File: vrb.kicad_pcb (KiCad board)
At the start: 6 copper layers, 82 x 75 mm, 217 parts, among them J1 SM04B-GHS, J10 MiniFit, J11 XT30, J12 Mezzanine, J13 MiniFit, J14 Conn_01x02, J2 SM04B-GHS, J3 MiniFit, J4 MiniFit, J5 Pixhawk 1, J6 Pixhawk 2, J7 SM04B-GHS, J8 DEBUG, J9 SM04B-GHS, Q1 Q_NMOS_GSD, Q2 Q_NMOS_GSD, U1 STM32G0B1CBUx, U10 INA180A2, U11 TJA1051TK/3/1J, U12 I3A4W008A033V-001-R, U13 INA180A2, U14 TPS2121, U15 TPS2121, U16 TLV71333PDBVR, U17 TLA2528, U18 TPS2116DRL, U2 TJA1051TK/3/1J, U3 LMR51635, U4 INA180A2, U5 LMR51635, U6 INA180A2, U7 LMR51635, U8 INA180A2, U9 LMR51635, Y1 XRCGB16M000FXN20R0

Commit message: improvements with derick
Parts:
- added D22: 15V, Diode_SMD:D_SOD-523, F.Cu at (116.7, 126.5)
- added Q3: MMBT5551L, Package_TO_SOT_SMD:SOT-23, F.Cu at (120.2, 127.6)
- added Q4: FDC5614P, Package_TO_SOT_SMD:TSOT-23-6, F.Cu at (139.8, 122.9)
- added R84: 10K, Resistor_SMD:R_0402_1005Metric, F.Cu at (120.3, 130.7)
- added R85: 1K, Resistor_SMD:R_0402_1005Metric, F.Cu at (123.2, 128.8)
- added TP10: TestPoint, TestPoint:TestPoint_Pad_1.0x1.0mm, F.Cu at (99.9, 129.3)
- added TP12: GND, TestPoint:TestPoint_Loop_D2.50mm_Drill1.0mm, F.Cu at (85.0, 65.0)
- D11, D4, D5, D6, D7: value BLUE -> GREEN
- R43: value Rup -> 8K2
- R78: value 330 -> 24K
- moved R81 1.25 mm to (143.4, 119.3)
- moved R82 1.25 mm to (143.4, 120.9)
- moved R83 1.25 mm to (143.4, 122.5)
- moved TP11 1.25 mm to (146.4, 122.0)
- moved D20 0.30 mm to (118.2, 130.8)
- moved R78 0.30 mm to (117.7, 132.2)
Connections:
- D20 pad 2: /FAULT -> Net-(D20-A)
- U1 pad 29: /FAULT -> /nFAULT
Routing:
- net Net-(D22-K): track 0.00 -> 30.5 mm, vias 0 -> 2
- net Net-(D20-A): track 0.00 -> 25.8 mm, vias 0 -> 2
- net /FAULT: track 9.91 -> 0.00 mm
- net /nFAULT: track 0.00 -> 6.31 mm
- net +3V3: track 340.4 -> 343.2 mm
- net GND: track 111.9 -> 114.6 mm, vias 149 -> 151
- net /RESV2: track 58.4 -> 60.2 mm
- net Net-(Q3-B): track 0.00 -> 1.68 mm
- net +BATT: track 0.78 -> 1.47 mm, vias 22 -> 24
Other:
- board text added: "GND"

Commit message: final export of r1 after changes
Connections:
- net /IPAYLOAD renamed /IPAYLOAD1
- net /RESV0 renamed /IPAYLOAD2
- net /RESV1 renamed /IPAYLOAD3
- net /RESV2 renamed /VBAT_SCALED

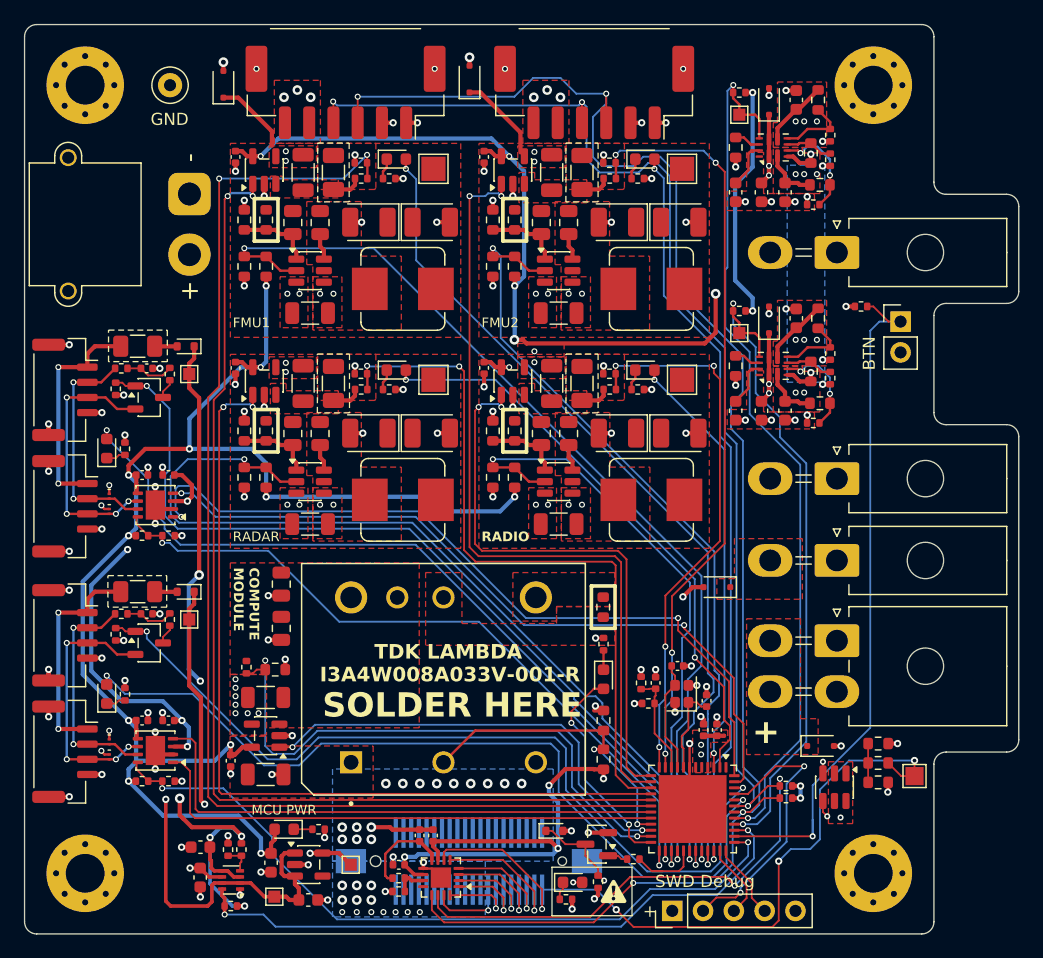
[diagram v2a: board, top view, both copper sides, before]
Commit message: updated layout for fault led with new circuit, rerouted
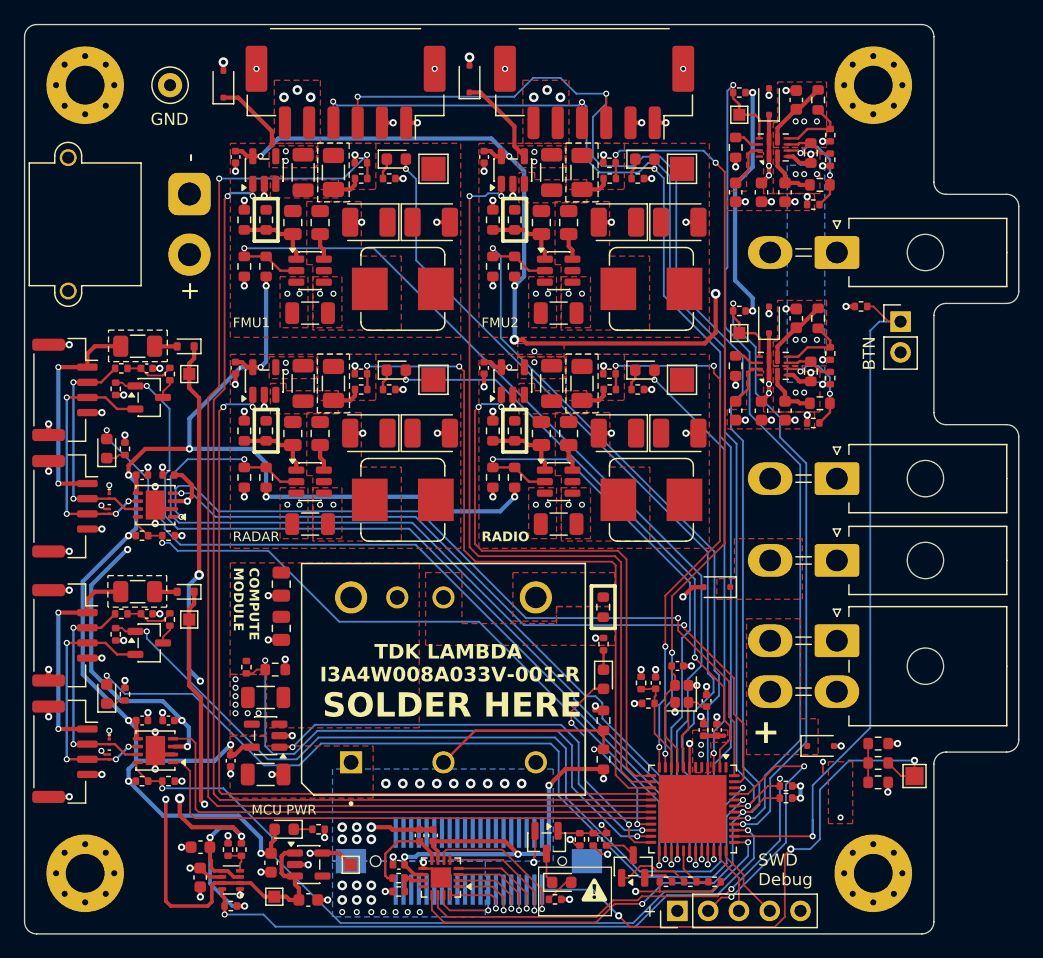
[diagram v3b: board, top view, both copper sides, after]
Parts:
- removed D22: 15V, Diode_SMD:D_SOD-523
- removed the Q4 at (139.8, 122.9)
- added Q3: BSS123, Package_TO_SOT_SMD:SOT-23, F.Cu at (116.0, 127.4)
- added R76: 200K, Resistor_SMD:R_0402_1005Metric, F.Cu at (119.9, 127.2)
- added R78: 1K, Resistor_SMD:R_0402_1005Metric, F.Cu at (121.0, 127.2)
- added R81: 20K, Resistor_SMD:R_0402_1005Metric, F.Cu at (129.9, 130.7)
- added R82: 180, Resistor_SMD:R_0402_1005Metric, F.Cu at (125.9, 130.7)
- R79: renamed from R84; value 10K -> 68K
- R80: renamed from R85; value 1K -> 5K
- moved R80 5.06 mm to (127.9, 130.7)
- moved R79 3.81 mm to (118.8, 127.2)
- moved Q4 3.52 mm to (123.2, 129.4), turned to 90 degrees
- moved D20 0.90 mm to (117.3, 130.8)
- moved R77 0.90 mm to (116.8, 132.2)
- moved J14 0.42 mm to (126.8, 133.1)
- renumbered C38 to C1, C7 to C10, C8 to C11, C48 to C12, C9 to C13, C10 to C14, C11 to C15, C12 to C16, C13 to C17, C49 to C18, C14 to C19, C39 to C2, C15 to C20, C16 to C21, C17 to C22, C18 to C23, C50 to C24, C19 to C25, C20 to C26, C21 to C27, C22 to C28, C23 to C29, C1 to C3, C51 to C30, C24 to C31, C25 to C32, C26 to C33, C27 to C34, C28 to C35, C29 to C36, C33 to C37, C34 to C38, C36 to C39, C2 to C4, C35 to C40, C30 to C41, C31 to C42, C37 to C43, C32 to C44, C44 to C45, C42 to C47, C54 to C48, C55 to C49, C3 to C5, C57 to C50, C43 to C51, C45 to C52, C40 to C53, C41 to C54, C47 to C6, C4 to C7, C5 to C8, C6 to C9, D9 to D10, D10 to D11, D19 to D12, D11 to D13, D13 to D14, D12 to D15, D15 to D16, D14 to D17, D16 to D18, D21 to D19, D18 to D21, D17 to D4, D4 to D5, D5 to D6, D6 to D7, D7 to D8, D8 to D9, J11 to J1, J5 to J10, J10 to J11, J6 to J12, J8 to J14, J12 to J2, J14 to J3, J1 to J4, J2 to J5, J7 to J6, J9 to J7, J4 to J8, J3 to J9, Q3 to Q4, R79 to R1, R9 to R10, R10 to R11, R11 to R12, R12 to R13, R13 to R14, R14 to R15, R15 to R16, R16 to R17, R17 to R18, R18 to R19, R1 to R2, R19 to R20, R20 to R21, R21 to R22, R22 to R23, R23 to R24, R24 to R25, R25 to R26, R26 to R27, R27 to R28, R28 to R29, R2 to R3, R29 to R30, R30 to R31, R31 to R32, R32 to R33, R33 to R34, R34 to R35, R35 to R36, R36 to R37, R37 to R38, R38 to R39, R3 to R4, R39 to R40, R40 to R41, R41 to R42, R42 to R43, R43 to R47, R4 to R5, R61 to R53, R62 to R54, R63 to R55, R64 to R56, R65 to R57, R66 to R58, R67 to R59, R5 to R6, R68 to R60, R56 to R61, R58 to R62, R59 to R63, R54 to R64, R57 to R65, R60 to R66, R53 to R67, R55 to R68, R73 to R69, R6 to R7, R75 to R70, R47 to R71, R69 to R72, R81 to R73, R82 to R74, R83 to R75, R78 to R77, R7 to R8, R71 to R83, R72 to R84, R74 to R85, R70 to R86, R77 to R87, R76 to R88, R8 to R9, TP12 to TP1, TP11 to TP10, TP10 to TP11, TP9 to TP12, TP5 to TP2, TP1 to TP3, TP2 to TP4, TP3 to TP5, TP4 to TP6, TP8 to TP7, TP7 to TP8, TP6 to TP9, U13 to U12, U12 to U13, U15 to U14, U14 to U15, U17 to U16, U16 to U17
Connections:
- Q4 pad 2: GND -> Net-(Q4-E)
- Q4 pad 3: Net-(D22-K) -> Net-(Q4-C)
- R77 pad 1: Net-(D20-K) -> Net-(D20-A)
- R77 pad 2: GND -> +BATT
- R79 pad 2: Net-(D22-K) -> Net-(Q3-G)
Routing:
- net Net-(D22-K): track 30.4 -> 0.00 mm, vias 2 -> 0
- net Net-(Q3-G): track 0.00 -> 26.3 mm, vias 0 -> 2
- net Net-(D20-A): track 25.8 -> 2.42 mm, vias 2 -> 0
- net GND: track 114.6 -> 122.9 mm
- net Net-(Q4-B): track 1.68 -> 6.09 mm
- net Net-(Q4-E): track 0.00 -> 2.58 mm
- net Net-(Q4-C): track 0.00 -> 2.53 mm
- net /nFAULT: track 6.31 -> 3.99 mm
- net +BATT: track 1.47 -> 2.95 mm, vias 24 -> 25
- net Net-(D20-K): track 1.51 -> 2.57 mm
- net /SWDIO: track 6.31 -> 5.62 mm
- net /USART1_TX_DEBUG: track 23.0 -> 22.4 mm
- net /I2C3_SDA_SMBUS: track 135.1 -> 134.5 mm
- net /SWCLK: track 6.28 -> 6.88 mm
- removed copper zone on F.Cu, net Net-(C27-Pad1)
